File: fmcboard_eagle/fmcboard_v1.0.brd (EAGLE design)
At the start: 98 x 74 mm, 63 parts, among them IC1 OPA699ID, IC2 OPA699ID, IC3 ICL7660CPA, IC4 ICL7660CPA, IC5 LM358, J1 8pin, J12 4p-2.54, J2 ASP-134604-01, J3 4p-2.54, J4 4p-2.54, J5 8pin, J6 4p-2.54, Q1 BSS138, Q2 BSS138, Q3 BSS138, Q4 BSS138

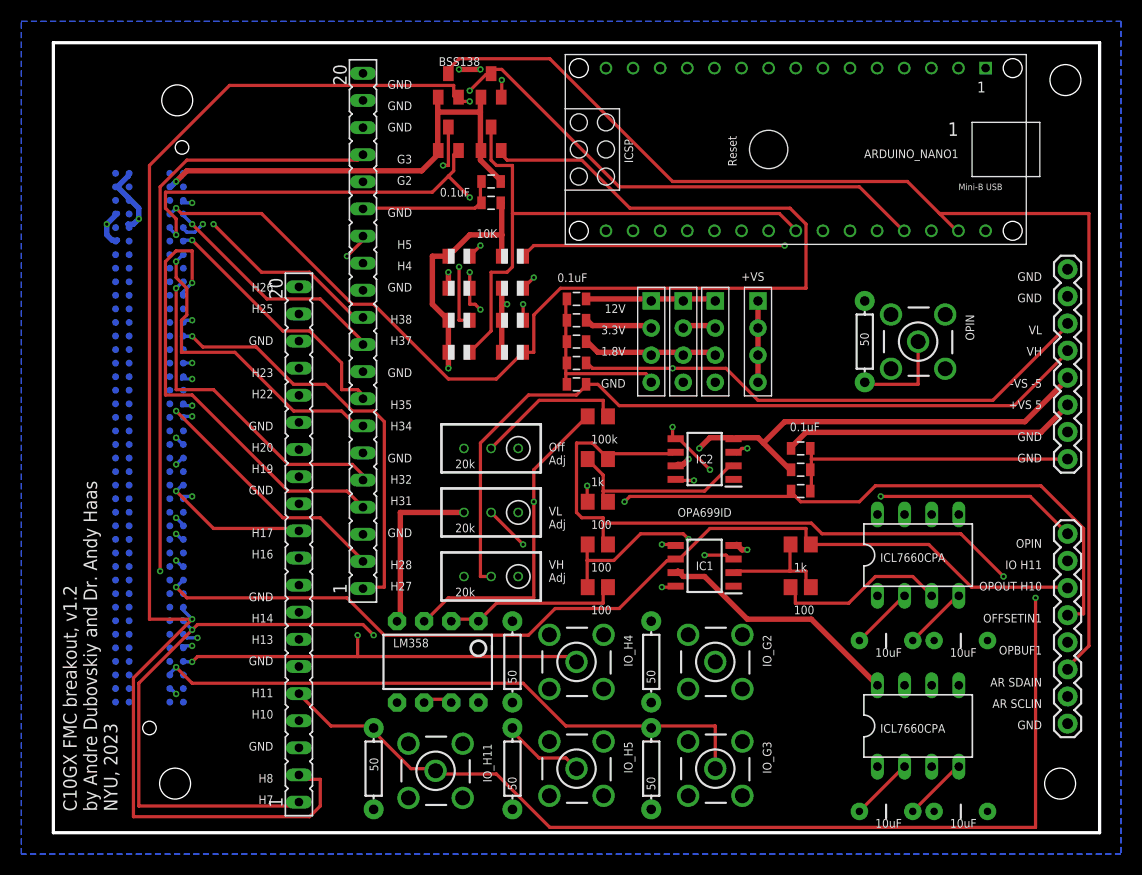
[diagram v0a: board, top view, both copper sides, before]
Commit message: Revert "use bss138 level shifting"
This reverts commit dd6467e355429a32c42db6855984b6cad7435a14.
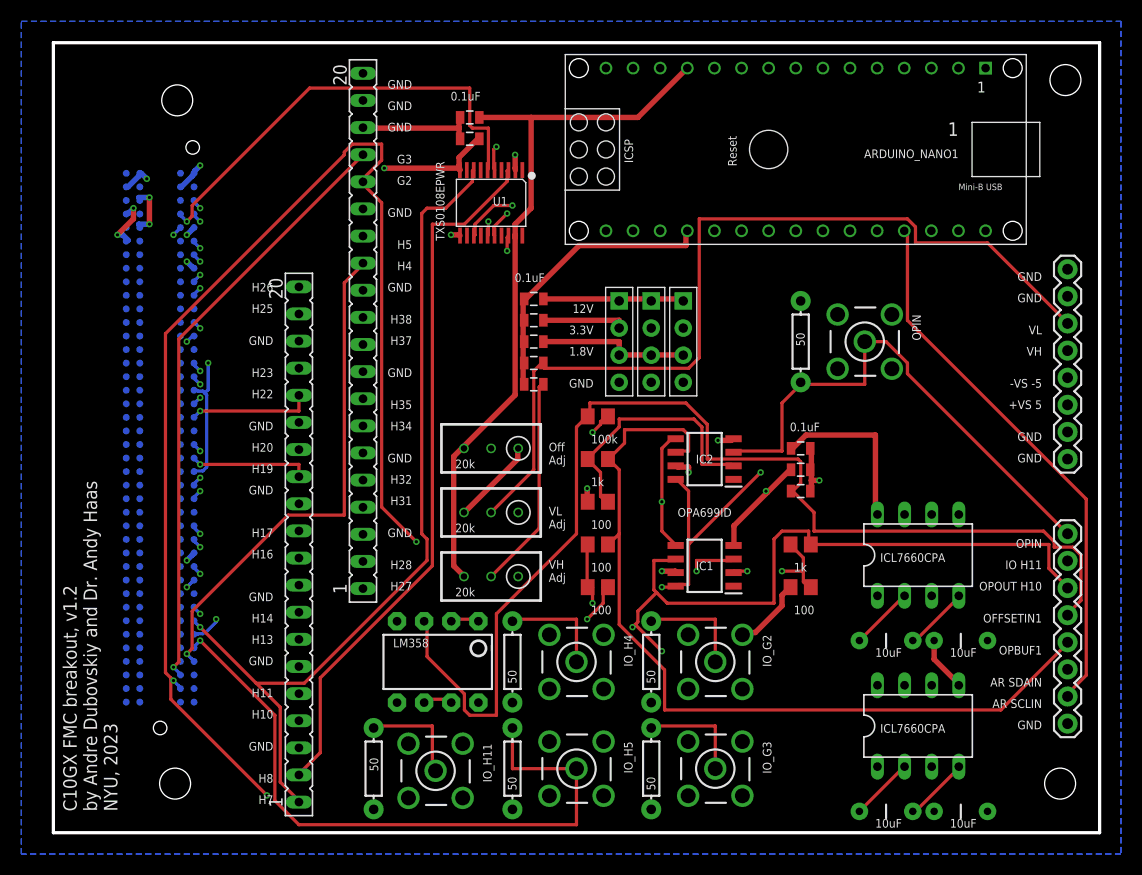
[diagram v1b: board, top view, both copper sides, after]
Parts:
- removed J6: 4p-2.54, Seeed-Connector:H4-2.54
- removed Q1, Q2, Q3, Q4: BSS138, adafruit:SOT23
- removed R17, R18, R19, R20, R21, R22, R23, R24: 10K, adafruit:R0805
- added U1: TXS0108EPWR, Seeed-IC:TSSOP20-0.65-6.5X4.4MM
- moved C9 8.25 mm to (39.0, 67.0)
- moved R2 6.00 mm to (70.0, 46.0)
- moved OPIN 5.00 mm to (76.0, 46.0)
- moved C14 4.47 mm to (39.0, 65.0)
- moved C12 4.00 mm to (45.0, 50.0)
- moved C13 4.00 mm to (45.0, 48.0)
- moved C5 4.00 mm to (45.0, 46.0)
- moved C7 4.00 mm to (45.0, 42.0)
- moved C8 4.00 mm to (45.0, 44.0)
- moved J12 3.00 mm to (53.0, 46.0)
- moved J3 3.00 mm to (59.0, 46.0)
- moved J4 3.00 mm to (56.0, 46.0)
- moved J2 1.00 mm to (10.0, 37.0)
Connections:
- net 1V8: now also U1.10, U1.2; no longer Q1.1, Q2.1, Q3.1, Q4.1, R18.1, R20.1, R22.1, R24.1
- net AR_G36: now also U1.16; no longer Q3.3, R21.2
- net AR_G37: now also U1.15; no longer Q4.3, R23.2
- net AR_SCLIN: now also U1.13; no longer Q1.3, R19.2
- net AR_SDAIN: now also U1.18; no longer Q2.3, R17.2
- net G36: now also U1.5; no longer Q3.2, R22.2
- net G37: now also U1.6; no longer Q4.2, R24.2
- net GND: now also U1.11
- net SCLIN: now also U1.8; no longer Q1.2, R20.2
- net SDAIN: now also U1.3; no longer Q2.2, R18.2
- net VS+: now also U1.19; no longer J6.1, J6.2, J6.3, J6.4, R17.1, R19.1, R21.1, R23.1
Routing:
- net G37: track 109.6 -> 42.5 mm
- net SDAIN: track 146.6 -> 87.6 mm, vias 3 -> 1
- net AR_SDAIN: track 154.6 -> 97.1 mm
- net VS+: track 235.2 -> 189.8 mm
- net AR_G36: track 73.2 -> 33.1 mm, vias 2 -> 1
- net G2: track 141.5 -> 177.4 mm, vias 1 -> 3
- net H5: track 87.3 -> 121.9 mm, vias 2 -> 1
- net SCLIN: track 115.9 -> 81.7 mm, vias 5 -> 1
- net AR_SCLIN: track 126.4 -> 94.4 mm, vias 2 -> 1
- net GND: track 80.7 -> 105.7 mm, vias 3 -> 8
- net 1V8: track 118.3 -> 96.1 mm
- net AR_G37: track 52.6 -> 31.0 mm, vias 0 -> 1
- net VL: track 90.9 -> 111.9 mm, vias 5 -> 1
- net VS-: track 163.8 -> 143.8 mm
- net 12V: track 88.6 -> 69.0 mm, vias 3 -> 2
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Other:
- board text removed: "+VS"
